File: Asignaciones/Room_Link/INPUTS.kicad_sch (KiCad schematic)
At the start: 0 parts

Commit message: ROOM-LINK update KICAD
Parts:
- added C1, C2, C3, C4: 0.1uF, Capacitor_SMD:C_0805_2012Metric_Pad1.18x1.45mm_HandSolder, symbol Device:C
- added D6, D7, D8, D9: LED, LED_SMD:LED_0805_2012Metric_Pad1.15x1.40mm_HandSolder, symbol Device:LED
- added Q1, Q2, Q3, Q4: FODM2705, nuevo simbolo:FODM2705, symbol FODM2705:FODM2705
- added R10, R15, R19, R9: 10, Resistor_SMD:R_0805_2012Metric_Pad1.20x1.40mm_HandSolder, symbol Device:R
- added R11, R13, R17, R21: 470, Resistor_SMD:R_0805_2012Metric_Pad1.20x1.40mm_HandSolder, symbol Device:R
- added R12, R16, R20, R6: 10k, Resistor_SMD:R_0805_2012Metric_Pad1.20x1.40mm_HandSolder, symbol Device:R
- added R14, R18, R7, R8: 330, Resistor_SMD:R_0805_2012Metric_Pad1.20x1.40mm_HandSolder, symbol Device:R
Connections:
- net CON-IN1+: now also Q1.2 (CATHODE)
- net CON-IN1-: now also R10.2
- net CON-IN2+: now also R9.2
- net CON-IN2-: now also Q2.2 (CATHODE)
- net CON-IN3+: now also Q3.2 (CATHODE)
- net CON-IN3-: now also R15.2
- net CON-IN4+: now also Q4.2 (CATHODE)
- net CON-IN4-: now also R19.2
- net INPUT_1MICRO: now also C1.1, D6.1 (K), Q1.4 (COLLECTOR), R6.2
- net INPUT_2MICRO: now also C2.1, D7.1 (K), Q2.4 (COLLECTOR), R12.2
- net INPUT_3MICRO: now also C3.1, D8.1 (K), Q3.4 (COLLECTOR), R16.2
- net INPUT_4MICRO: now also C4.1, D9.1 (K), Q4.4 (COLLECTOR), R20.2
- new net: D7.2 (A), R13.2
- new net: Q2.1 (ANODE), R8.2
- new net: Q4.1 (ANODE), R18.2
- new net: Q1.1 (ANODE), R7.2
- new net: D8.2 (A), R17.2
- new net: D9.2 (A), R21.2
- new net: D6.2 (A), R11.2
- new net: Q3.1 (ANODE), R14.2
- new net +5V: R11.1, R12.1, R13.1, R16.1, R17.1, R20.1, R21.1, R6.1
- new net Earth: R10.1, R15.1, R19.1, R9.1
- new net GND: C1.2, C2.2, C3.2, C4.2, Q1.3 (EMITTER), Q2.3 (EMITTER), Q3.3 (EMITTER), Q4.3 (EMITTER)
- new net VDD: R14.1, R18.1, R7.1, R8.1

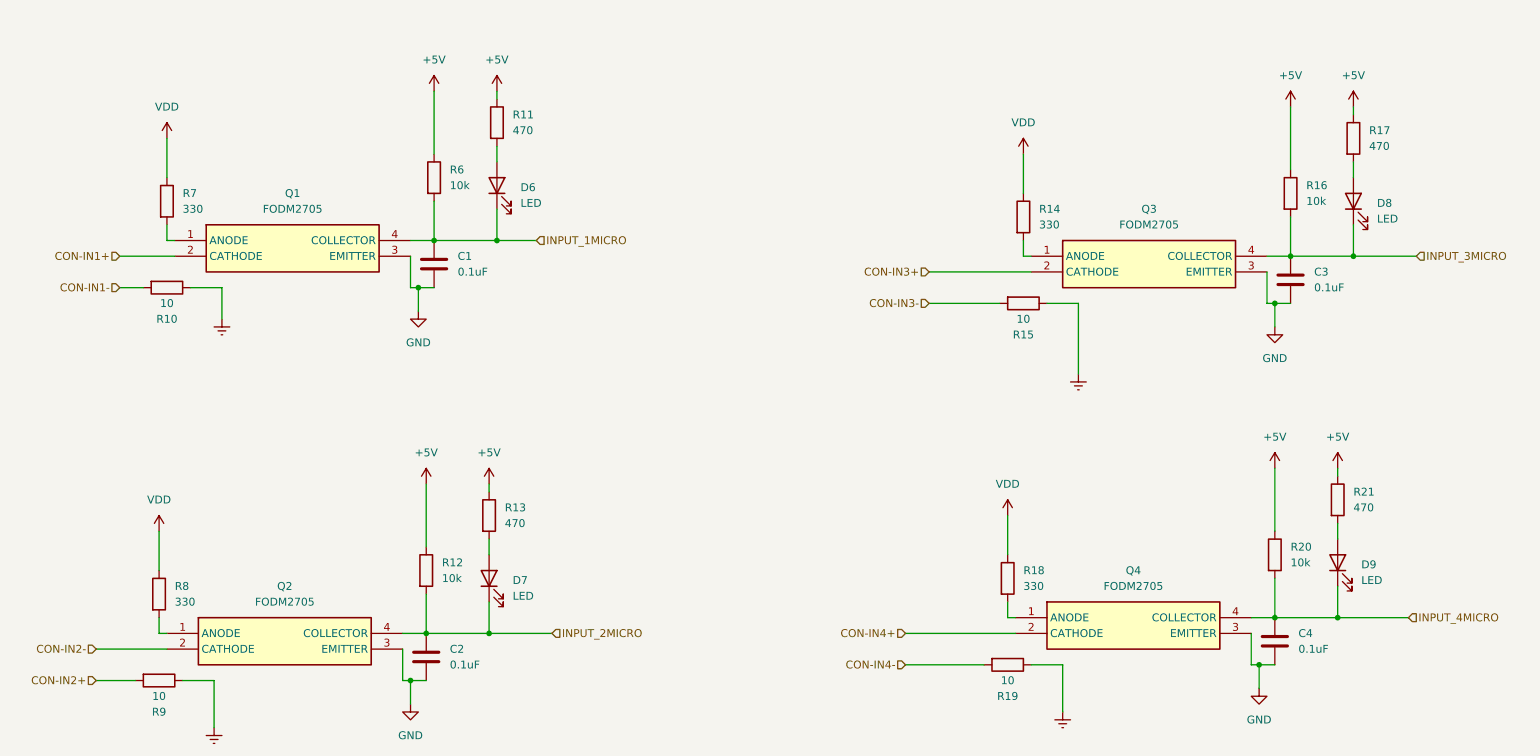
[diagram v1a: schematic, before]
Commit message: Place component Added & routing
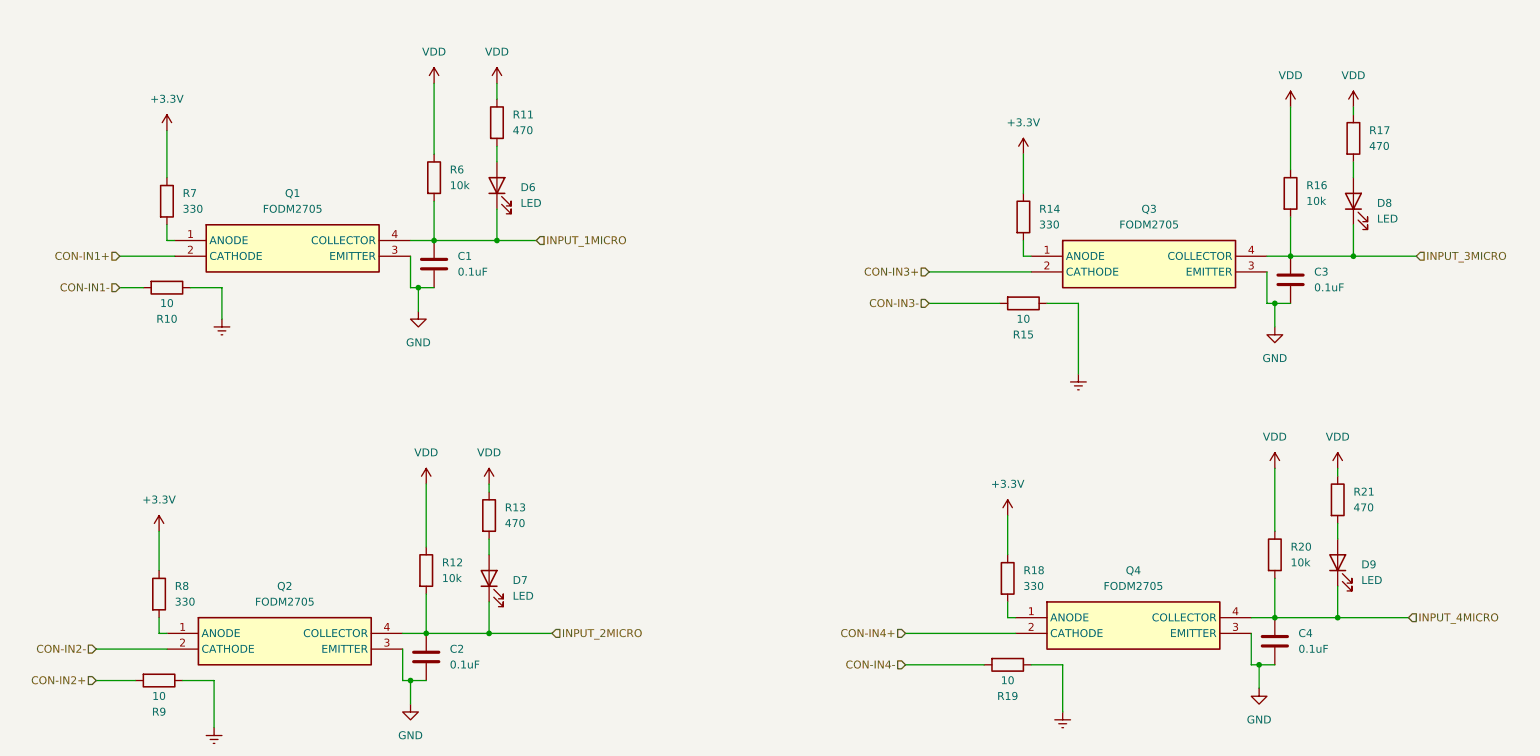
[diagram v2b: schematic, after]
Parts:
- C4: footprint Capacitor_SMD:C_0805_2012Metric_Pad1.18x1.45mm_HandSolder -> Capacitor_SMD:C_0805_2012Metric
- D6, D7, D8, D9: footprint LED_SMD:LED_0805_2012Metric_Pad1.15x1.40mm_HandSolder -> LED_SMD:LED_0805_2012Metric
- R10, R11, R12, R13, R14, R15, R16, R17, R18, R19, R20, R21, R6, R7, R8, R9: footprint Resistor_SMD:R_0805_2012Metric_Pad1.20x1.40mm_HandSolder -> Resistor_SMD:R_0805_2012Metric
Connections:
- net +5V is gone; now on net VDD: R11.1, R12.1, R13.1, R16.1, R17.1, R20.1, R21.1, R6.1
- net VDD: no longer R14.1, R18.1, R7.1, R8.1
- new net +3.3V: R14.1, R18.1, R7.1, R8.1
